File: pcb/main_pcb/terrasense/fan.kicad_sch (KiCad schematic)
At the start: 18 parts, among them J5 FAN0, J6 FAN1, Q10 MMBT2222A, Q5 MMBT2222A, Q6 BSS84, Q7 MMBT2222A, Q8 MMBT2222A, Q9 BSS84

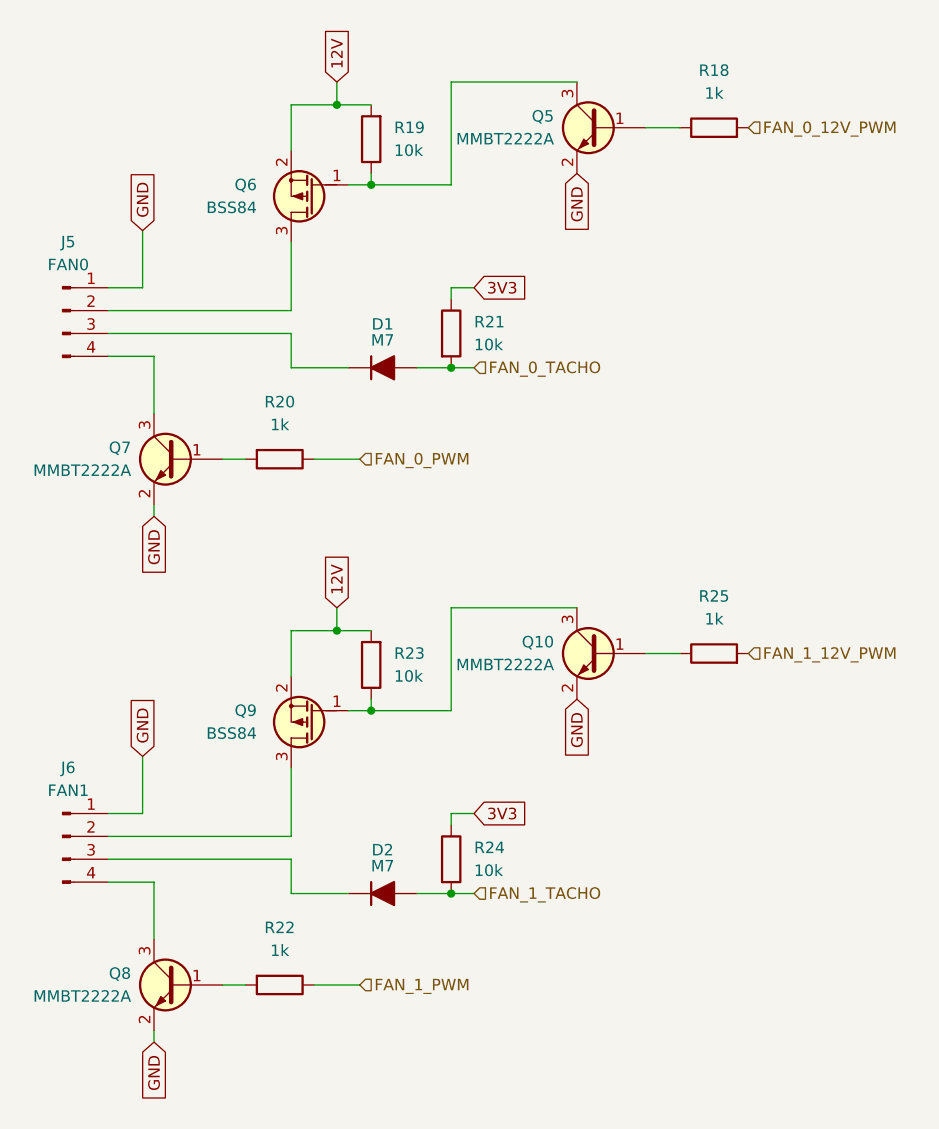
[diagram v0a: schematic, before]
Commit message: update pcb with ordered pcb
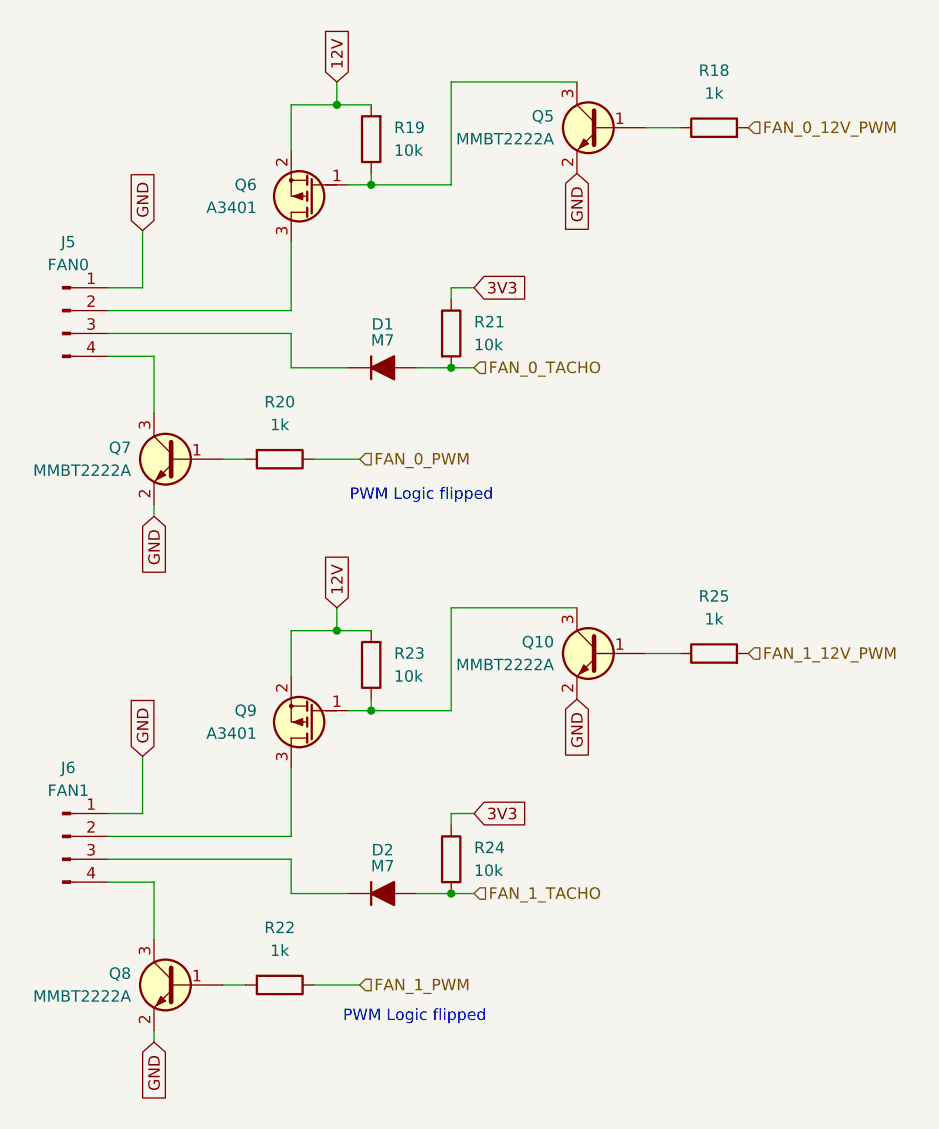
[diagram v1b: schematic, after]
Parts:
- Q6, Q9: value BSS84 -> A3401
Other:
- note added: "PWM Logic flipped"
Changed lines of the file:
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@@
 	(generator_version "10.0")
 	(paper "A4")
+	(text "PWM Logic flipped"
+		(exclude_from_sim no)
+		(at 90.678 66.294 0)
+		(effects
+			(font
+				(size 1.27 1.27)
+			)
+		)
+	)
+	(text "PWM Logic flipped"
+		(exclude_from_sim no)
+		(at 89.916 124.206 0)
+		(effects
+			(font
+				(size 1.27 1.27)
+			)
+		)
+	)
 	(junction
 		(at 93.98 52.07)
@@
 			)
 		)
-		(property "Value" "BSS84"
+		(property "Value" "A3401"
 			(at 72.39 34.2899 0)
 			(show_name no)
@@
 			)
 		)
-		(property "Datasheet" "https://www.tme.eu/Document/9e18544e3c24e82da23d9bbccfec4cfd/BSS84-FAI-DTE.pdf"
+		(property "Datasheet" ""
 			(at 78.74 33.02 0)
 			(hide yes)
@@
 			)
 		)
-		(property "Description" "SOT-23 P-MOSFET enchancement mode transistor, 50V, 130mA, 360mW, Alternate KiCAD Library"
+		(property "Description" "SOT-23 P-MOSFET enchancement mode transistor, 50V, up to 4A"
 			(at 78.74 33.02 0)
 			(hide yes)
@@
 			)
 		)
-		(property "Value" "BSS84"
+		(property "Value" "A3401"
 			(at 72.39 92.7099 0)
 			(show_name no)
@@
 			)
 		)
-		(property "Datasheet" "https://www.tme.eu/Document/9e18544e3c24e82da23d9bbccfec4cfd/BSS84-FAI-DTE.pdf"
+		(property "Datasheet" ""
 			(at 78.74 91.44 0)
 			(hide yes)
@@
 			)
 		)
-		(property "Description" "SOT-23 P-MOSFET enchancement mode transistor, 50V, 130mA, 360mW, Alternate KiCAD Library"
+		(property "Description" "SOT-23 P-MOSFET enchancement mode transistor, up to 4A"
 			(at 78.74 91.44 0)
 			(hide yes)
